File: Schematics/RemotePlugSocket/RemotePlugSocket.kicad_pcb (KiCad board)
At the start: 2 copper layers, 83.8 x 52.1 mm, 12 parts, among them J1 BME280, J2 Relay_Module, J3 LED_Status, J4 1-Wire CH1, J5 Power, J6 Button, U1 ESP32-DevKitC

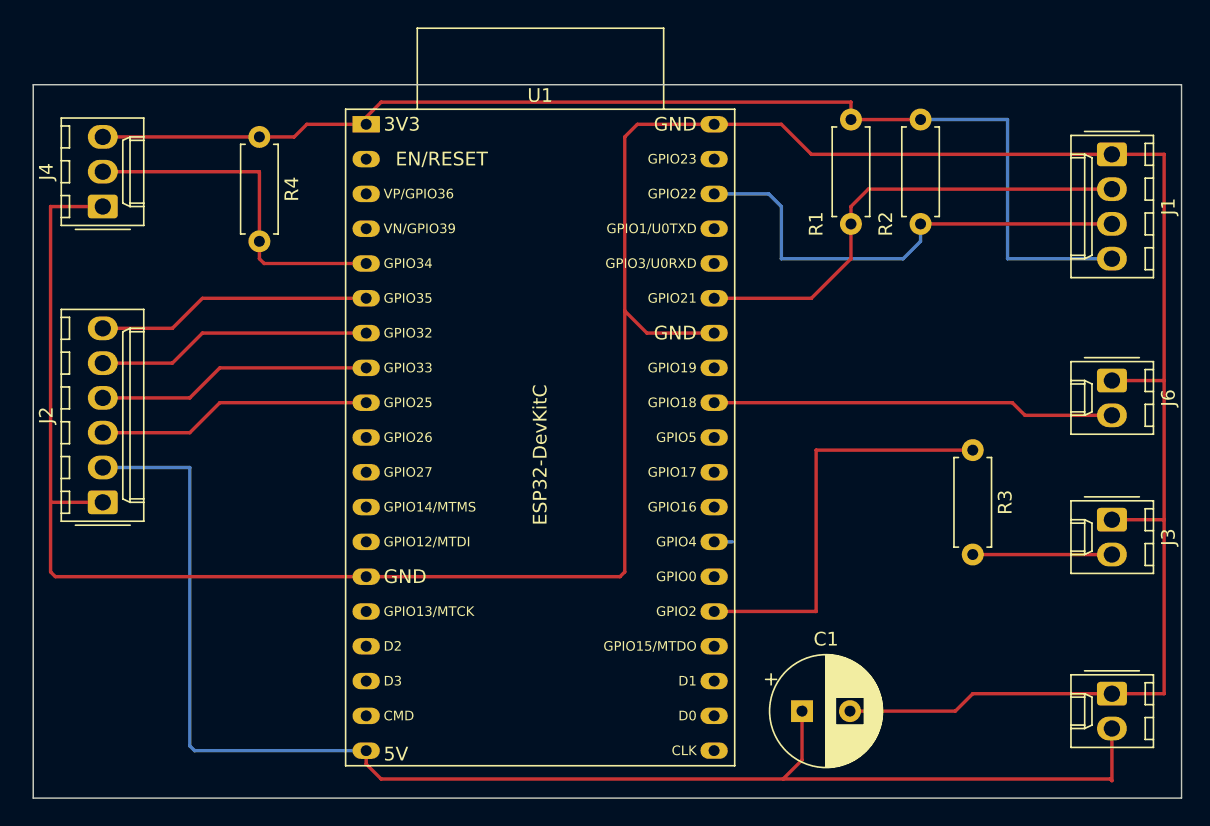
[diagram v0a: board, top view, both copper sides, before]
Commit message: Relay switching from HA now works.
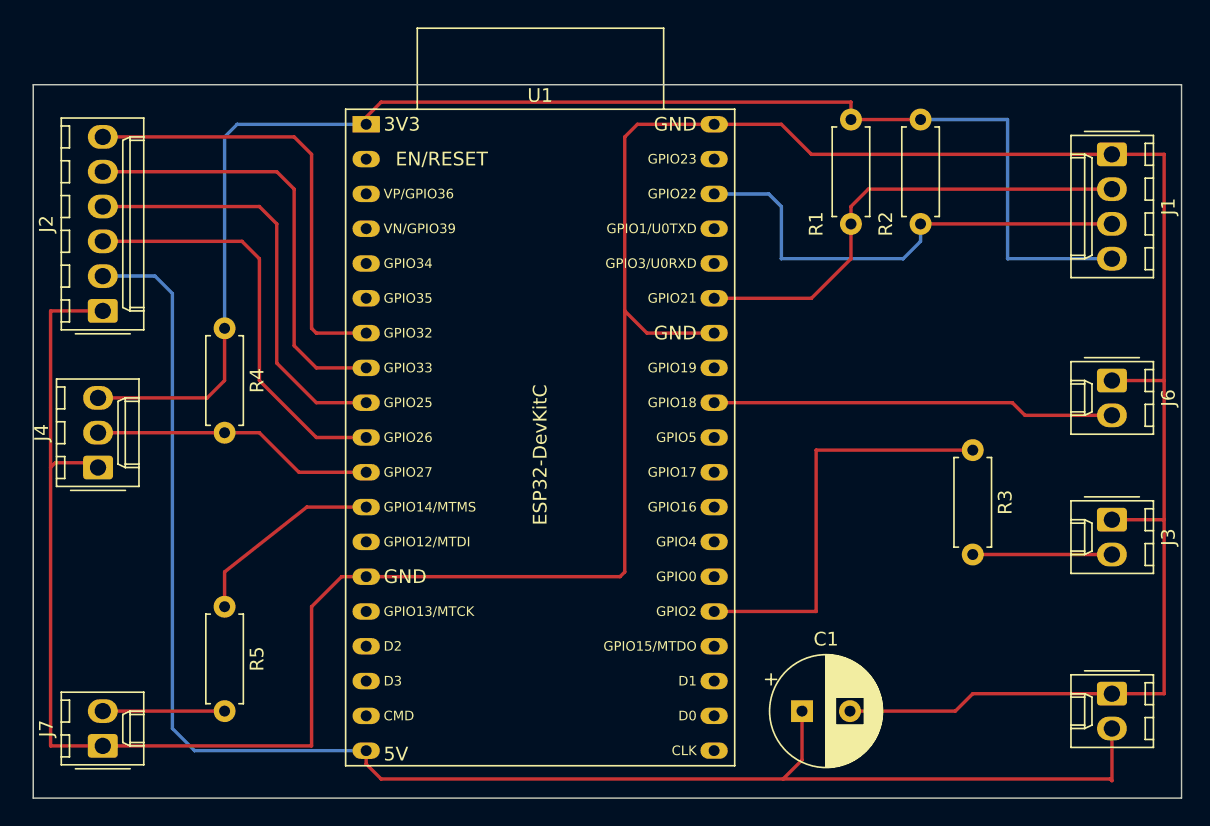
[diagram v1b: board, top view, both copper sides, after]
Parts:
- added J7: LED_Debug, Connector_Molex:Molex_KK-254_AE-6410-02A_1x02_P2.54mm_Vertical, F.Cu at (114.3, 111.8)
- added R5: 330, Resistor_THT:R_Axial_DIN0207_L6.3mm_D2.5mm_P7.62mm_Horizontal, F.Cu at (123.2, 101.6)
- moved J4 19.1 mm to (114.0, 91.4)
- moved R4 14.2 mm to (123.2, 81.3)
- moved J2 14.0 mm to (114.3, 80.0)
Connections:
- U1 pad 10: unconnected-(U1-DAC_2/ADC2_CH9/GPIO26-Pad10) -> RELAY_1
- U1 pad 11: unconnected-(U1-ADC2_CH7/GPIO27-Pad11) -> CH1_OneWire
- U1 pad 12: unconnected-(U1-MTMS/GPIO14/ADC2_CH6-Pad12) -> LED_Debug
- U1 pad 5: CH1_OneWire -> unconnected-(U1-VDET_1/GPIO34/ADC1_CH6-Pad5)
- U1 pad 6: RELAY_4 -> unconnected-(U1-VDET_2/GPIO35/ADC1_CH7-Pad6)
- U1 pad 7: RELAY_3 -> RELAY_4
- U1 pad 8: RELAY_2 -> RELAY_3
- U1 pad 9: RELAY_1 -> RELAY_2
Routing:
- net +3V3: track 86.4 -> 105.1 mm
- net GND: track 226.5 -> 242.3 mm
- net LED_Debug: track 0.00 -> 14.5 mm
- net +5V: track 104.9 -> 117.4 mm
- net RELAY_4: track 20.1 -> 32.6 mm
- net RELAY_3: track 20.1 -> 31.9 mm
- net RELAY_2: track 20.1 -> 31.1 mm
- net RELAY_1: track 20.1 -> 30.4 mm
- net Net-(J7-Pin_2): track 0.00 -> 8.89 mm
- net CH1_OneWire: track 25.7 -> 20.8 mm
- net unconnected-(U1-ADC2_CH0/GPIO4-Pad26): track 1.33 -> 0.00 mm
